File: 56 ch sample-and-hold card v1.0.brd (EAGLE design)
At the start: 160 x 24.8 mm, 116 parts, among them IC1 4051D, IC10 TL074JT, IC11 4051D, IC12 TL074JT, IC13 TL074JT, IC14 4051D, IC15 TL074JT, IC16 TL074JT, IC17 4051D, IC18 TL074JT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

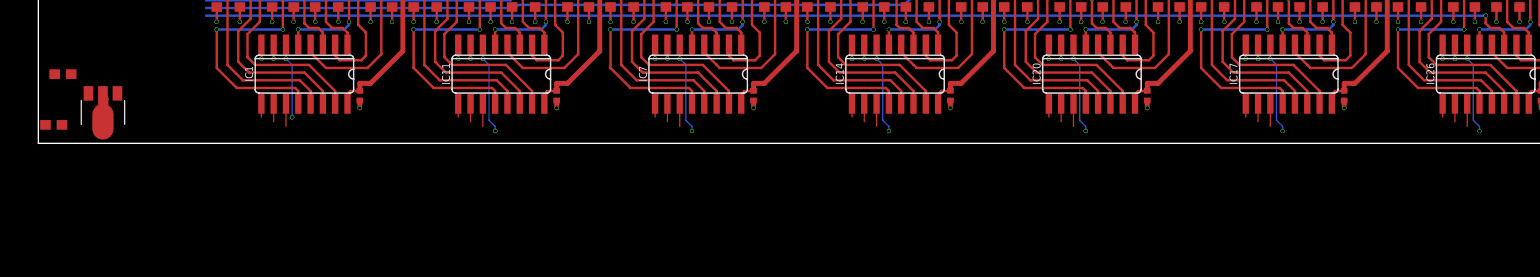
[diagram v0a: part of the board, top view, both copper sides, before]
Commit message: All cells for 56ch CV routed
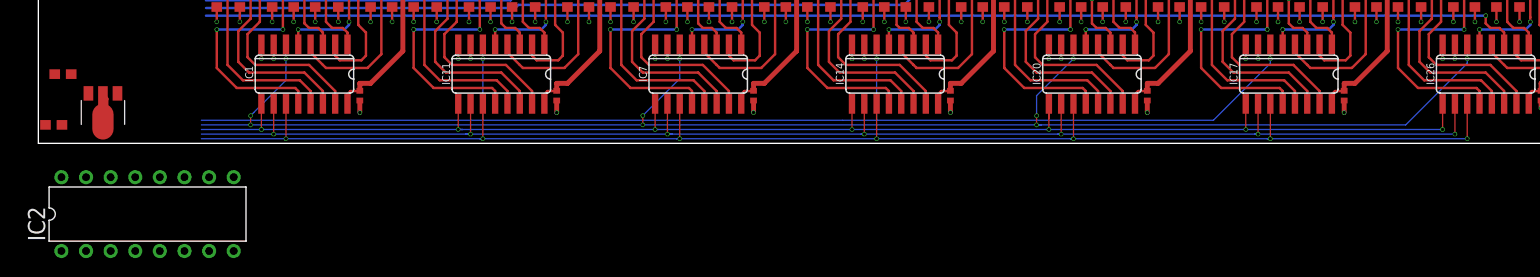
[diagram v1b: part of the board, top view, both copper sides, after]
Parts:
- added IC2: DAC8586D, joakim:DIL16J
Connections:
- new net AVDD: IC2.4
- new net IOVDD: IC2.12
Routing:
- net A0: track 16.3 -> 157.1 mm, vias 0 -> 7
- net A1: track 12.9 -> 153.1 mm, vias 0 -> 7
- net A2: track 9.60 -> 149.6 mm, vias 0 -> 7
- net INH_1: track 36.2 -> 165.3 mm, vias 8 -> 10
- net INH_2: track 28.4 -> 130.4 mm, vias 6 -> 3
- net AGND: track 137.4 -> 140.3 mm

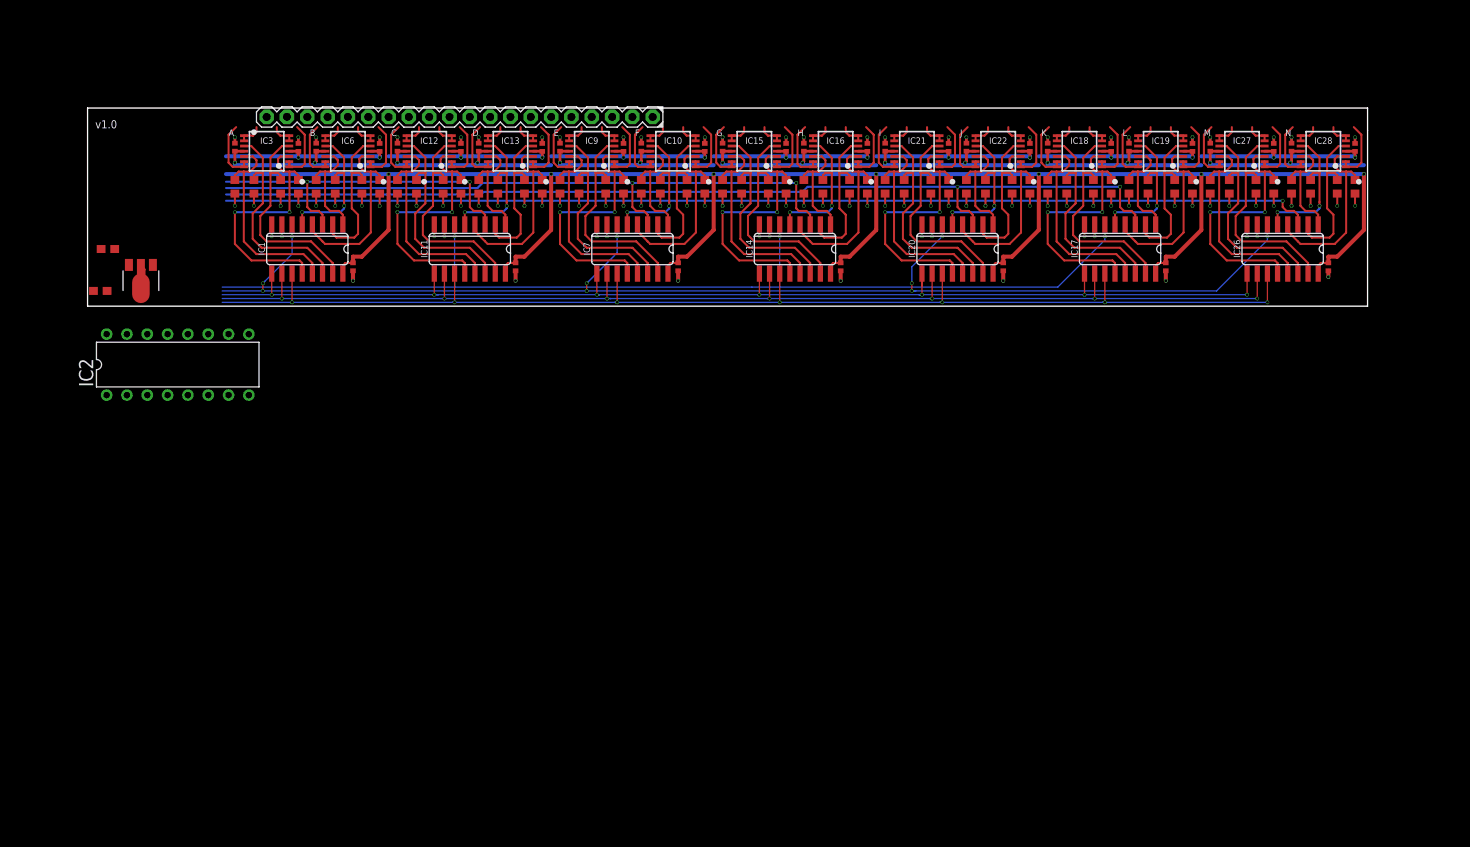
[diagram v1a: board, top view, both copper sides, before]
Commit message: Mostly routed, needs DAC testing
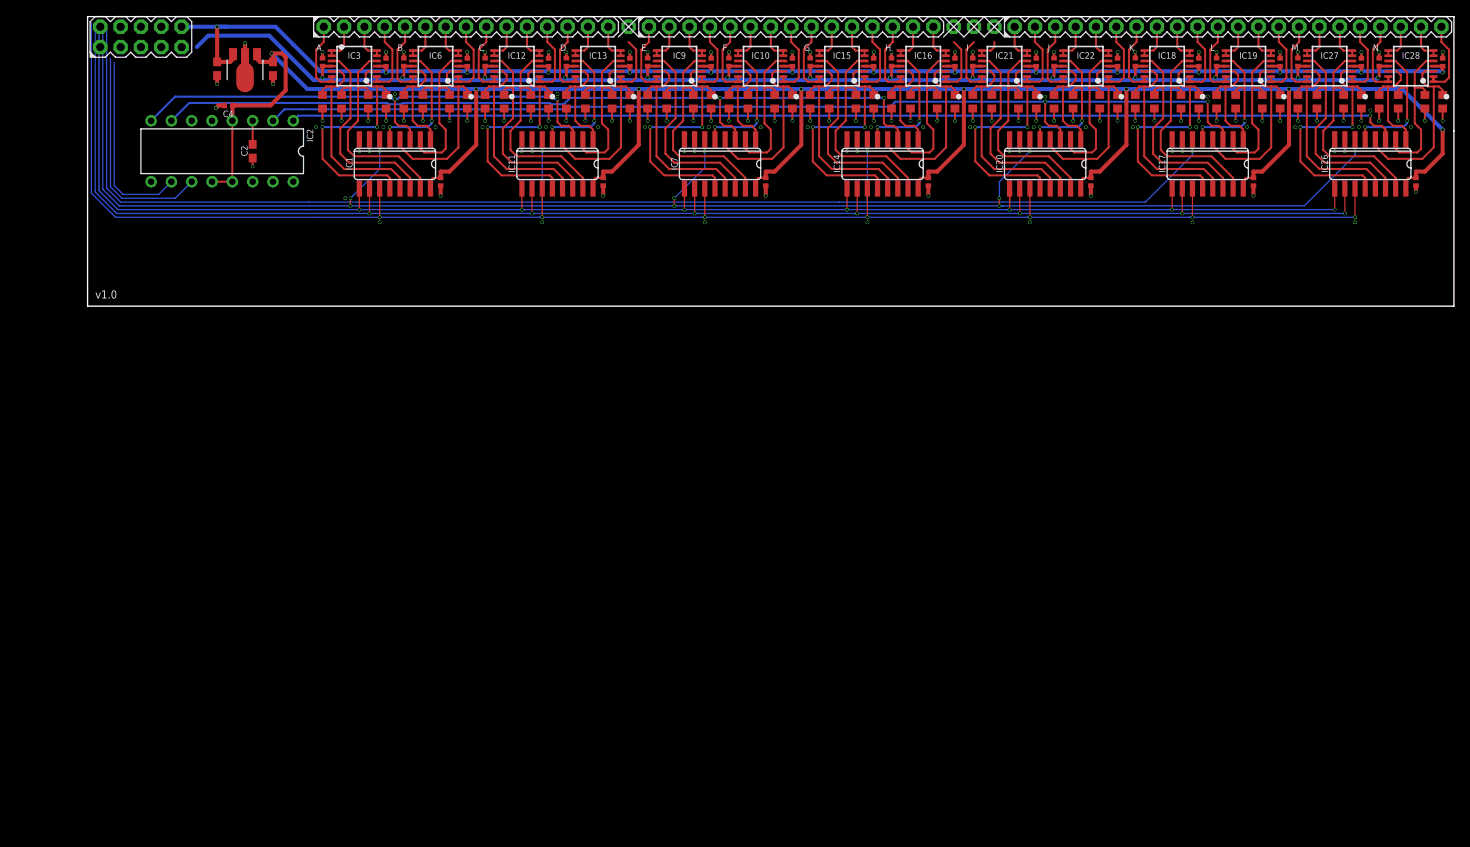
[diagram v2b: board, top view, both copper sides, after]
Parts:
- removed SV2: (no value), joakim:MA20-1
- added C2: 150nF, resistor:C0603
- added C4: (no value), joakim:C0402-J
- added X1: (no value), joakim:MA05-2J
- added X2, X3: FEMALE, joakim:MA15-1J
- added X4: FEMALE, joakim:MA22-1J
- added X5: DNM, joakim:MA01N-1J
- added X6: DNM, joakim:MA03N-1J
- moved C3 31.4 mm to (16.2, 29.7), turned to 90 degrees
- moved C1 30.6 mm to (23.2, 29.7), turned to 90 degrees
- moved IC5 29.4 mm to (19.7, 29.5)
- moved IC2 27.2 mm to (16.8, 19.4), turned to 180 degrees
- moved C107 15.3 mm to (166.1, 15.6)
- moved C116 15.3 mm to (163.8, 25.6)
- moved C76 15.3 mm to (146.8, 25.6)
- moved C82 15.3 mm to (118.6, 25.6)
- moved C85 15.3 mm to (110.6, 25.6)
- moved C86 15.3 mm to (118.6, 30.5)
- moved C87 15.3 mm to (110.6, 30.5)
- moved C89 15.3 mm to (126.5, 25.6)
- moved IC17 15.3 mm to (140.0, 17.8)
- moved IC21 15.3 mm to (114.6, 30.0)
- moved IC26 15.3 mm to (160.3, 17.8)
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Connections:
- removed net AVDD: IC2.4
- removed net IOVDD: IC2.12
- new net N$8: C2.2, IC2.3
- new net SCK: IC2.10
- new net SDA: IC2.11
- net +12V: no longer SV2.18
- net +5V: now also C4.1, IC2.12, IC2.13, IC2.4
- net -12V: no longer SV2.19
- net AGND: now also C2.1, C4.2, IC2.14, IC2.15, IC2.16, IC2.5, IC2.6, IC2.9; no longer SV2.17
- net DAC_1: now also IC2.1, IC26.3; no longer IC1.3, IC11.3
- net DAC_2: now also IC17.3, IC2.2, IC20.3; no longer IC14.3, IC7.3
- net DAC_3: now also IC14.3, IC2.7, IC7.3; no longer IC17.3, IC20.3
- net DAC_4: now also IC1.3, IC11.3, IC2.8; no longer IC26.3
- net OUT_0: now also X2.1; no longer SV2.1
- net OUT_1: now also X2.2; no longer SV2.2
- net OUT_10: now also X2.11; no longer SV2.11
- net OUT_11: now also X2.12; no longer SV2.12
- net OUT_12: now also X2.13; no longer SV2.13
- net OUT_13: now also X2.14; no longer SV2.14
- net OUT_14: now also X2.15; no longer SV2.15
- net OUT_15: now also X5.1; no longer SV2.16
- net OUT_16: now also X3.1
- net OUT_17: now also X3.2
- net OUT_18: now also X3.3
- net OUT_19: now also X3.4
- net OUT_2: now also X2.3; no longer SV2.3
- net OUT_20: now also X3.5
- net OUT_21: now also X3.6
- net OUT_22: now also X3.7
- net OUT_23: now also X3.8
- net OUT_24: now also X3.9
- net OUT_25: now also X3.10
- net OUT_26: now also X3.11
- net OUT_27: now also X3.12
- net OUT_28: now also X3.13
- net OUT_29: now also X3.14
- net OUT_3: now also X2.4; no longer SV2.4
- net OUT_30: now also X3.15
- net OUT_31: now also X6.1
- net OUT_32: now also X6.2
- net OUT_33: now also X6.3
- net OUT_34: now also X4.1
- net OUT_35: now also X4.2
- net OUT_36: now also X4.3
- net OUT_37: now also X4.4
- net OUT_38: now also X4.5
- net OUT_39: now also X4.6
- net OUT_4: now also X2.5; no longer SV2.5
- net OUT_40: now also X4.7
- net OUT_41: now also X4.8
- net OUT_42: now also X4.9
- net OUT_43: now also X4.10
- net OUT_44: now also X4.11
- net OUT_45: now also X4.12
- net OUT_46: now also X4.13
- net OUT_47: now also X4.14
- net OUT_48: now also X4.15
- net OUT_49: now also X4.16
- net OUT_5: now also X2.6; no longer SV2.6
- net OUT_50: now also X4.17
- net OUT_51: now also X4.18
- net OUT_52: now also X4.19
- net OUT_53: now also X4.20
- net OUT_54: now also X4.21
- net OUT_55: now also X4.22
- net OUT_6: now also X2.7; no longer SV2.7
- net OUT_7: now also X2.8; no longer SV2.8
- net OUT_8: now also X2.9; no longer SV2.9
- net OUT_9: now also X2.10; no longer SV2.10
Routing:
- net DAC_1: track 43.9 -> 139.2 mm, vias 2 -> 1
- net DAC_4: track 136.4 -> 65.2 mm, vias 1 -> 2
- net A0: track 157.1 -> 206.9 mm
- net A1: track 153.1 -> 202.0 mm
- net A2: track 149.6 -> 197.7 mm
- net INH_1: track 165.3 -> 212.7 mm
- net INH_2: track 130.4 -> 177.0 mm
- net DAC_2: track 84.5 -> 129.9 mm
- net +12V: track 163.6 -> 196.6 mm, vias 14 -> 15
- net +5V: track 254.3 -> 286.2 mm, vias 7 -> 8
- net SDA: track 0.00 -> 27.6 mm
- net SCK: track 0.00 -> 23.7 mm
- net DAC_3: track 124.3 -> 103.5 mm
- net -12V: track 175.4 -> 191.3 mm
- net N$8: track 0.00 -> 2.96 mm
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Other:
- board size 160 x 24.8 mm -> 170.8 x 36.2 mm
- board text removed: "+"
- board text removed: "-"
